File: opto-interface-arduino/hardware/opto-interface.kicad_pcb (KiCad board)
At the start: 2 copper layers, 11 parts, among them P1 CONN_02X06, U1 LM7805, U2 LM7905

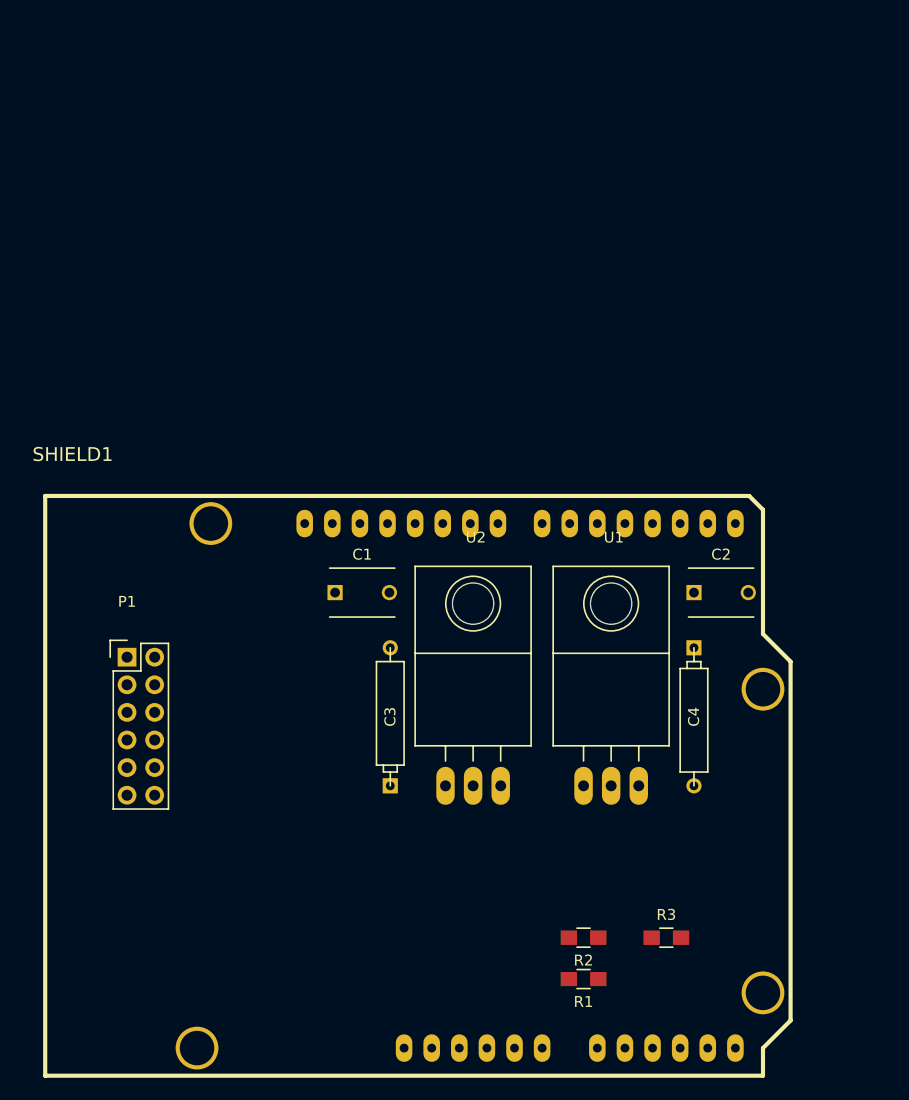
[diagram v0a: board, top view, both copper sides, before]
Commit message: Update to include external power connector.
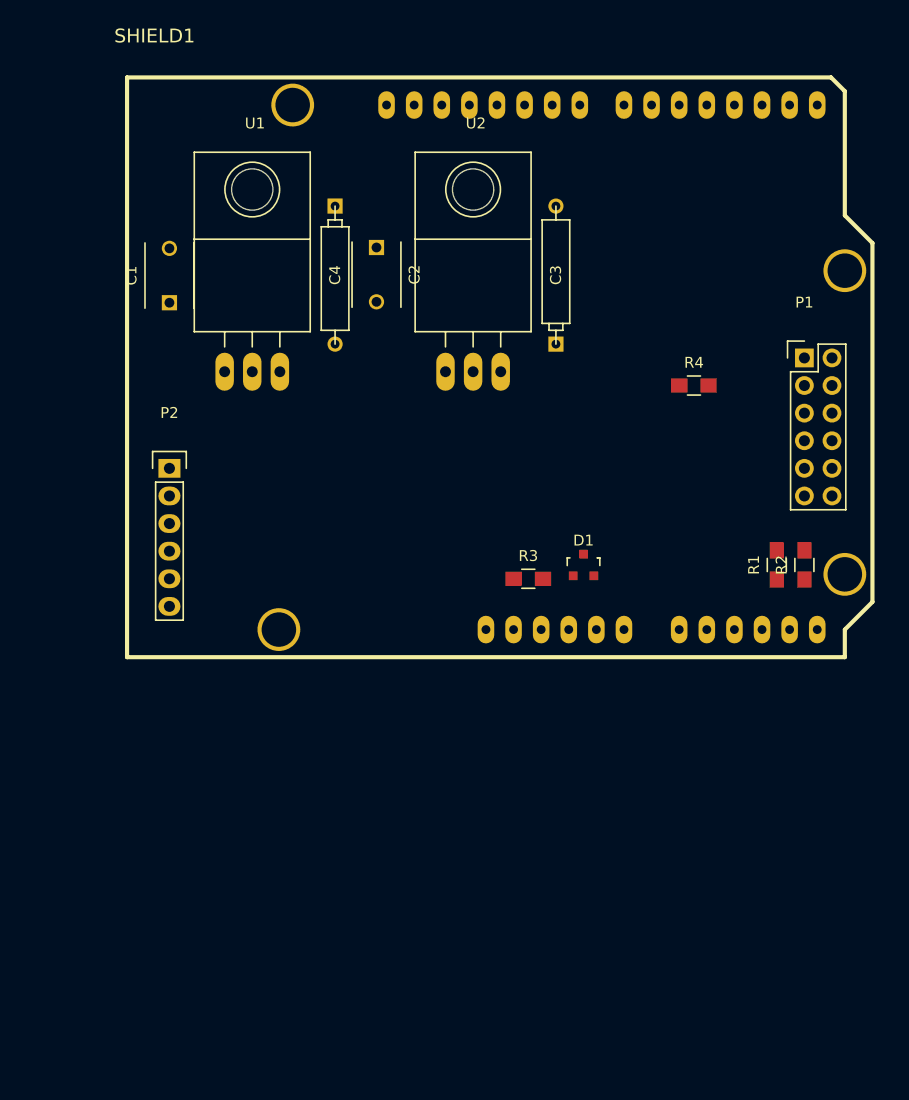
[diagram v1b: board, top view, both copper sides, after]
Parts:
- added D1: ZENER, TO_SOT_Packages_SMD:SOT-23, F.Cu at (190.5, 96.5)
- added P2: CONN_01X06, Pin_Headers:Pin_Header_Straight_1x06, F.Cu at (152.4, 87.6)
- added R4: 390R, Resistors_SMD:R_0805_HandSoldering, F.Cu at (200.7, 80.0)
- R3: value 390R -> 1k3R
- moved P1 68.1 mm to (210.8, 77.5)
- moved C4 52.4 mm to (167.6, 69.8)
- moved U1 50.4 mm to (160.0, 78.7)
- moved C3 43.4 mm to (188.0, 69.8)
- moved C2 43.1 mm to (171.4, 67.3), turned to 270 degrees
- moved R1 42.0 mm to (208.3, 96.5), turned to 90 degrees
- moved R2 39.9 mm to (210.8, 96.5), turned to 90 degrees
- moved SHIELD1 39.2 mm to (148.5, 105.0)
- moved U2 38.1 mm to (180.3, 78.7)
- moved R3 35.4 mm to (185.4, 97.8)
- moved C1 30.7 mm to (152.4, 72.4), turned to 90 degrees
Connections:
- R3 pad 1: +5V -> +3V3
- R3 pad 2: Net-(P1-Pad5) -> Net-(D1-Pad1)
- SHIELD1 pad 3V3: Net-(SHIELD1-Pad3V3) -> +3V3
- SHIELD1 pad AREF: Net-(SHIELD1-PadAREF) -> Net-(D1-Pad1)

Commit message: Add filter simulations, first pass layout, some calculations and some skeleton code.
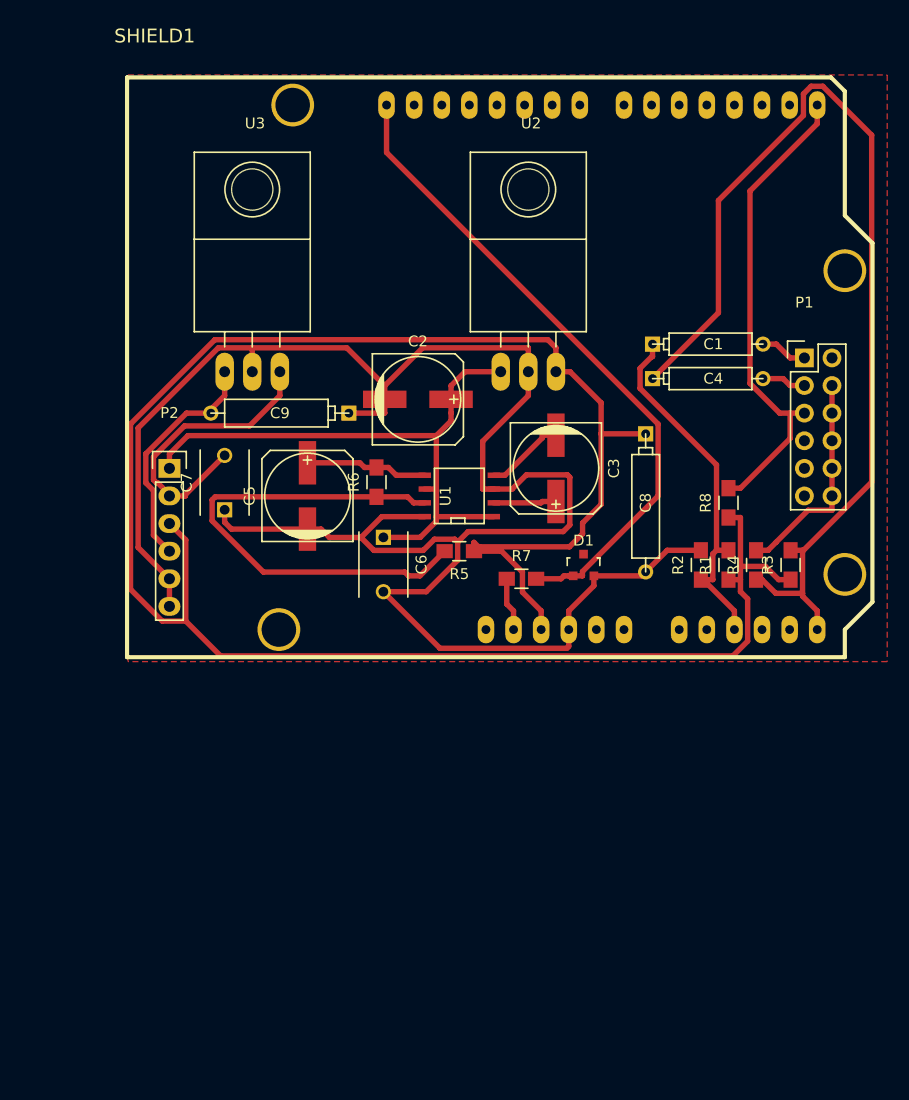
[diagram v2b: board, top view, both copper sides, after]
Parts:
- added C5: 4u7F, Capacitors_SMD:c_elec_8x5.4, F.Cu at (165.1, 90.2)
- added C6: 0u1F, Capacitors_ThroughHole:C_Disc_D6_P5, F.Cu at (172.1, 94.0)
- added C7: 0u1F, Capacitors_ThroughHole:C_Disc_D6_P5, F.Cu at (157.5, 91.4)
- added C8: 2u2F, Discret:CP5, F.Cu at (196.2, 90.8)
- added C9: 2u2F, Discret:CP5, F.Cu at (162.6, 82.5)
- added R5: 100kR, Resistors_SMD:R_0805_HandSoldering, F.Cu at (179.1, 95.2)
- added R6: 100kR, Resistors_SMD:R_0805_HandSoldering, F.Cu at (171.4, 88.9)
- added R7: 1k3R, Resistors_SMD:R_0805_HandSoldering, F.Cu at (184.8, 97.8)
- added R8: 390R, Resistors_SMD:R_0805_HandSoldering, F.Cu at (203.8, 90.8)
- added U3: LM7905, regul:TO-220_regul_Horizontal_LargePads, F.Cu at (160.0, 78.7)
- C1: value 0u1F -> 10uF; footprint Capacitors_ThroughHole:C_Disc_D6_P5 -> Discret:CP4
- C2: value 0u1F -> CP; footprint Capacitors_ThroughHole:C_Disc_D6_P5 -> Capacitors_SMD:c_elec_8x5.4
- C3: value 2u2F -> CP; footprint Discret:CP5 -> Capacitors_SMD:c_elec_8x5.4
- C4: value 2u2F -> 10uF; footprint Discret:CP5 -> Discret:CP4
- R1: value 100kR -> 750kR
- R3: value 1k3R -> 750kR
- R4: value 390R -> 100kR
- U1: value LM7805 -> max889; footprint TO_SOT_Packages_THT:TO-220_Neutral123_Horizontal_LargePads -> SMD_Packages:SOIC-8-N
- U2: value LM7905 -> LM7805; footprint TO_SOT_Packages_THT:TO-220_Neutral123_Horizontal_LargePads -> regul:TO-220_regul_Horizontal_LargePads
- moved C1 49.7 mm to (201.9, 76.2), turned to 0 degrees
- moved C4 35.6 mm to (201.9, 79.4), turned to 0 degrees
- moved R3 24.2 mm to (209.6, 96.5), turned to 90 degrees
- moved U1 22.2 mm to (179.1, 90.2), turned to 90 degrees
- moved C3 17.8 mm to (188.0, 87.6), turned to 270 degrees
- moved R4 17.5 mm to (206.4, 96.5), turned to 90 degrees
- moved C2 14.5 mm to (175.3, 81.3), turned to 0 degrees
- moved R2 9.53 mm to (201.3, 96.5)
- moved U2 5.08 mm to (185.4, 78.7)
- moved R1 4.44 mm to (203.8, 96.5)
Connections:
- C1 pad 1: +12V -> Net-(C1-Pad1)
- C1 pad 2: GND -> Net-(C1-Pad2)
- C2 pad 1: GND -> +12V
- C2 pad 2: -12V -> GND
- C3 pad 1: +5V -> Net-(C3-Pad1)
- C3 pad 2: GND -> Net-(C3-Pad2)
- C4 pad 1: GND -> Net-(C4-Pad1)
- C4 pad 2: -5V -> Net-(C4-Pad2)
- P1 pad 1: Net-(P1-Pad1) -> Net-(C1-Pad2)
- P1 pad 2: GND -> Net-(P1-Pad2)
- P1 pad 3: Net-(P1-Pad3) -> Net-(C4-Pad2)
- P1 pad 7: +5V -> Net-(P1-Pad7)
- P1 pad 9: -5V -> Net-(P1-Pad9)
- R1 pad 1: Net-(P1-Pad1) -> +5V
- R1 pad 2: GND -> Net-(C1-Pad1)
- R2 pad 1: Net-(P1-Pad3) -> Net-(C1-Pad1)
- R3 pad 1: +3V3 -> +5V
- R3 pad 2: Net-(D1-Pad1) -> Net-(C4-Pad1)
- R4 pad 1: +5V -> Net-(C4-Pad1)
- R4 pad 2: Net-(P1-Pad5) -> GND
- SHIELD1 pad AD2: Net-(SHIELD1-PadAD2) -> Net-(C1-Pad1)
- SHIELD1 pad AD4: Net-(P1-Pad1) -> Net-(SHIELD1-PadAD4)
- SHIELD1 pad AD5: Net-(P1-Pad3) -> Net-(C4-Pad1)
- U1 pad 1: (no net) -> +12V
- U1 pad 2: (no net) -> Net-(C3-Pad1)
- U1 pad 3: (no net) -> GND
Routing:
- net GND: track 0.00 -> 204.3 mm
- net +5V: track 0.00 -> 193.4 mm
- net Net-(C4-Pad1): track 0.00 -> 95.0 mm
- net Net-(D1-Pad1): track 0.00 -> 60.9 mm
- net +12V: track 0.00 -> 56.5 mm
- net Net-(R5-Pad2): track 0.00 -> 46.3 mm
- net Net-(P1-Pad5): track 0.00 -> 44.2 mm
- net Net-(C1-Pad1): track 0.00 -> 33.1 mm
- net -12V: track 0.00 -> 27.1 mm
- net -5V: track 0.00 -> 21.7 mm
- net Net-(C5-Pad1): track 0.00 -> 11.3 mm
- net Net-(C3-Pad2): track 0.00 -> 7.38 mm
- net Net-(C3-Pad1): track 0.00 -> 5.77 mm
- net +3V3: track 0.00 -> 4.93 mm
- net Net-(C1-Pad2): track 0.00 -> 4.34 mm
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- added copper zone on F.Cu, net GND

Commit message: Complete v 0.1 layout
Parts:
- moved C8 11.8 mm to (189.2, 81.3), turned to 180 degrees
- moved R1 10.4 mm to (195.6, 90.2)
- moved C7 9.53 mm to (157.5, 101.0)
- moved C1 9.09 mm to (200.0, 85.1)
- moved C4 7.65 mm to (207.0, 85.1), turned to 90 degrees
- moved C6 5.85 mm to (168.3, 89.5), turned to 90 degrees
- moved R3 5.39 mm to (205.7, 92.7), turned to 0 degrees
- moved R4 4.49 mm to (210.8, 97.2)
- moved C5 3.86 mm to (161.3, 89.5)
- moved R2 2.84 mm to (203.8, 97.8), turned to 0 degrees
- moved R8 2.54 mm to (201.3, 90.8)
- moved R6 2.01 mm to (173.4, 89.5)
- moved U2 1.27 mm to (185.4, 77.5)
- moved U3 1.27 mm to (160.0, 77.5)
- moved C3 0.90 mm to (188.6, 88.3)
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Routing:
- net +5V: track 193.4 -> 95.7 mm
- net GND: track 204.3 -> 284.4 mm
- net Net-(C4-Pad1): track 95.0 -> 15.4 mm
- net Net-(D1-Pad1): track 60.9 -> 99.6 mm
- net Net-(R5-Pad2): track 46.3 -> 8.90 mm
- net Net-(C1-Pad2): track 4.34 -> 11.9 mm
- net Net-(C5-Pad1): track 11.3 -> 18.1 mm
- net Net-(P1-Pad5): track 44.2 -> 49.0 mm
- net -12V: track 27.1 -> 31.2 mm
- net +12V: track 56.5 -> 54.4 mm
- net -5V: track 21.7 -> 23.7 mm
- net +3V3: track 4.93 -> 3.41 mm
- net Net-(C1-Pad1): track 33.1 -> 31.9 mm
- net Net-(C3-Pad1): track 5.77 -> 6.56 mm
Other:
- board outline added: 70.5 x 54 mm
- net class Default: clearance 0.2 -> 0.4
- rule trace_clearance: 0.2 -> 0.4

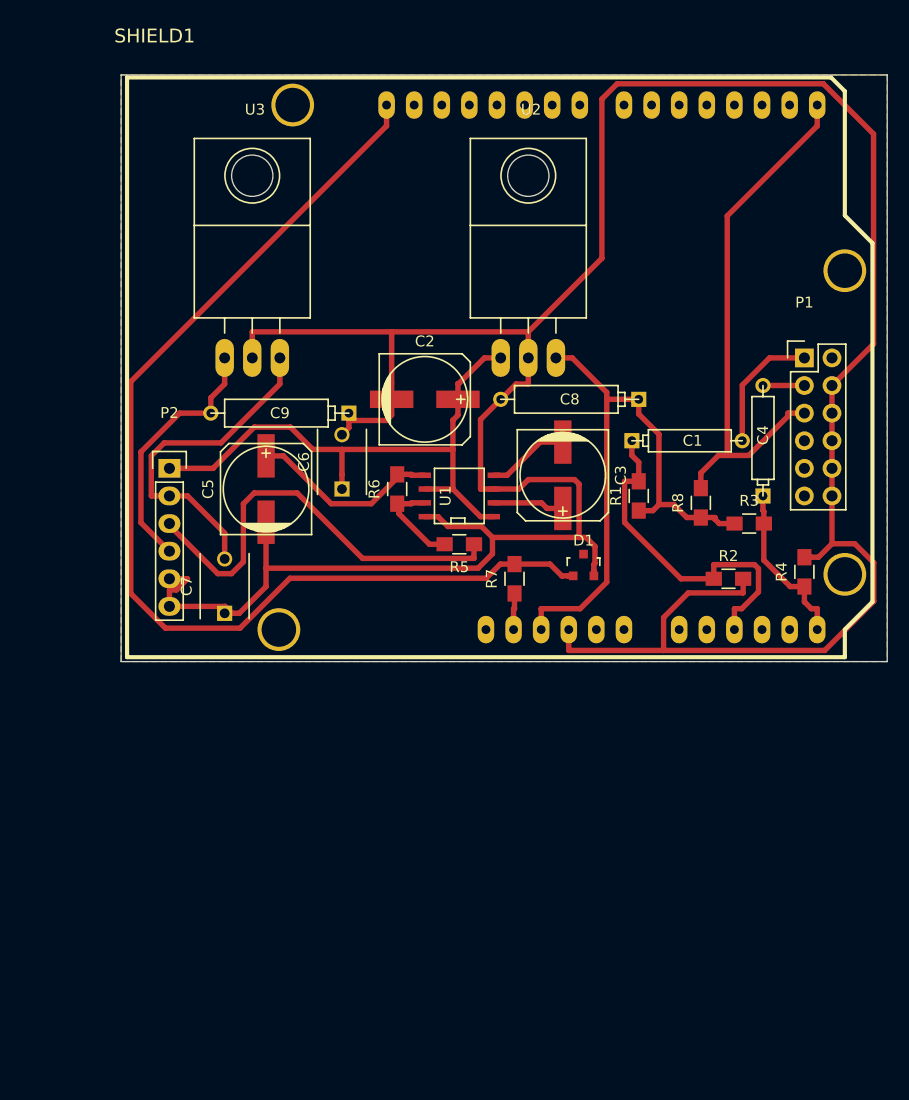
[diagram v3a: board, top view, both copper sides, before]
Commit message: Modify layout to ahem follow the datasheet guidance on MAX889. Update analogue input schematic for simulation to accomodate steeper low-pass roll-off.
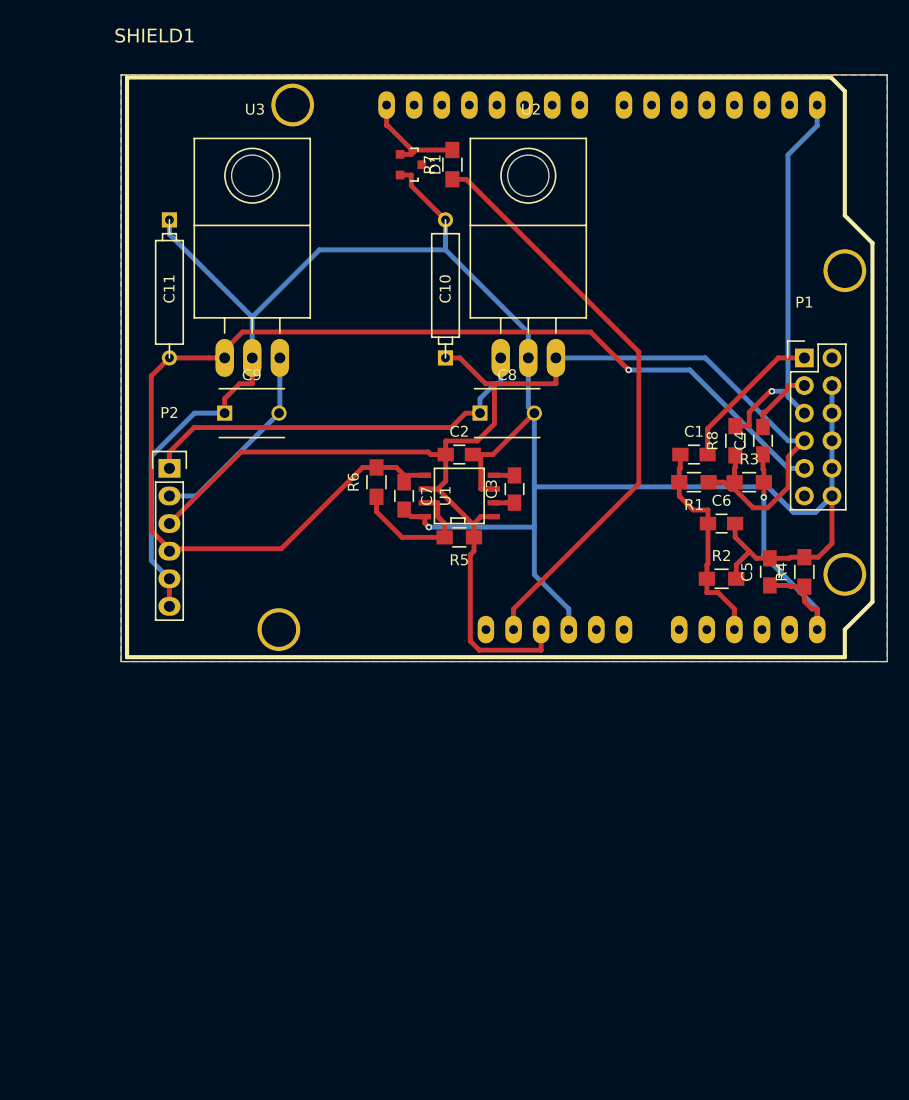
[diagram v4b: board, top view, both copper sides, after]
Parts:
- added C10: 2u2F, Discret:CP5, F.Cu at (177.8, 71.1)
- added C11: 2u2F, Discret:CP5, F.Cu at (152.4, 71.1)
- C1, C4: footprint Discret:CP4 -> Capacitors_SMD:C_0805_HandSoldering
- C2: value CP -> 10uF; footprint Capacitors_SMD:c_elec_8x5.4 -> Capacitors_SMD:C_0805_HandSoldering
- C3: value CP -> 2u2F; footprint Capacitors_SMD:c_elec_8x5.4 -> Capacitors_SMD:C_0805_HandSoldering
- C5: value 4u7F -> 1nF; footprint Capacitors_SMD:c_elec_8x5.4 -> Capacitors_SMD:C_0805_HandSoldering
- C6: value 0u1F -> 1nF; footprint Capacitors_ThroughHole:C_Disc_D6_P5 -> Capacitors_SMD:C_0805_HandSoldering
- C7: value 0u1F -> 10uF; footprint Capacitors_ThroughHole:C_Disc_D6_P5 -> Capacitors_SMD:C_0805_HandSoldering
- C8, C9: value 2u2F -> 0u1F; footprint Discret:CP5 -> Capacitors_ThroughHole:C_Disc_D6_P5
- R1, R3: value 750kR -> 100kR
- moved C5 47.0 mm to (207.6, 97.2)
- moved D1 40.1 mm to (174.6, 59.7), turned to 270 degrees
- moved R7 38.5 mm to (178.4, 59.7)
- moved C6 35.1 mm to (203.2, 92.7), turned to 0 degrees
- moved C7 19.7 mm to (174.0, 90.2), turned to 270 degrees
- moved C8 8.35 mm to (181.0, 82.5), turned to 0 degrees
- moved R8 6.54 mm to (204.5, 85.1)
- moved C2 5.99 mm to (179.1, 86.4)
- moved R1 5.24 mm to (200.7, 88.9), turned to 180 degrees
- moved C9 5.08 mm to (157.5, 82.5), turned to 0 degrees
- moved C3 4.62 mm to (184.2, 89.5), turned to 90 degrees
- moved R3 3.81 mm to (205.7, 88.9)
- moved R6 2.01 mm to (171.4, 88.9)
- moved C1 1.42 mm to (200.7, 86.4)
- moved R2 0.64 mm to (203.2, 97.8)
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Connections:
- C2 pad 1: +12V -> +5V
- C5 pad 1: Net-(C5-Pad1) -> Net-(C4-Pad1)
- C6 pad 1: +12V -> Net-(C1-Pad1)
- C7 pad 1: GND -> -5V
- C7 pad 2: -12V -> GND
- C8 pad 1: +5V -> +12V
- C9 pad 2: -5V -> -12V
- P1 pad 7: Net-(P1-Pad7) -> +5V
- P1 pad 9: Net-(P1-Pad9) -> -5V
- R6 pad 2: Net-(C5-Pad1) -> -5V
- U1 pad 1: +12V -> +5V
- U1 pad 5: Net-(C5-Pad1) -> -5V
- U1 pad 6: +12V -> +5V
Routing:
- net Net-(D1-Pad1): track 99.6 -> 10.4 mm
- net -5V: track 23.7 -> 112.0 mm, vias 0 -> 1
- net GND: track 284.4 -> 197.5 mm, vias 0 -> 1
- net +3V3: track 3.41 -> 54.1 mm
- net +5V: track 95.7 -> 126.1 mm
- net Net-(C5-Pad1): track 18.1 -> 0.00 mm
- net +12V: track 54.4 -> 37.7 mm
- net -12V: track 31.2 -> 18.3 mm
- net Net-(C1-Pad1): track 31.9 -> 19.8 mm
- net Net-(P1-Pad5): track 49.0 -> 37.0 mm, vias 0 -> 1
- net Net-(C4-Pad1): track 15.4 -> 26.1 mm, vias 0 -> 1
- net Net-(C3-Pad2): track 7.61 -> 1.91 mm
- net Net-(C3-Pad1): track 6.56 -> 1.91 mm
- net Net-(R5-Pad2): track 8.90 -> 13.3 mm
- net Net-(C4-Pad2): track 3.81 -> 6.40 mm
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- added copper zone on B.Cu, net GND
